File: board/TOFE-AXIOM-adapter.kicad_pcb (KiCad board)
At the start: 4 copper layers, 68.9 x 28.3 mm, 11 parts, among them CN1 C, U1 24AA01/24LC01B

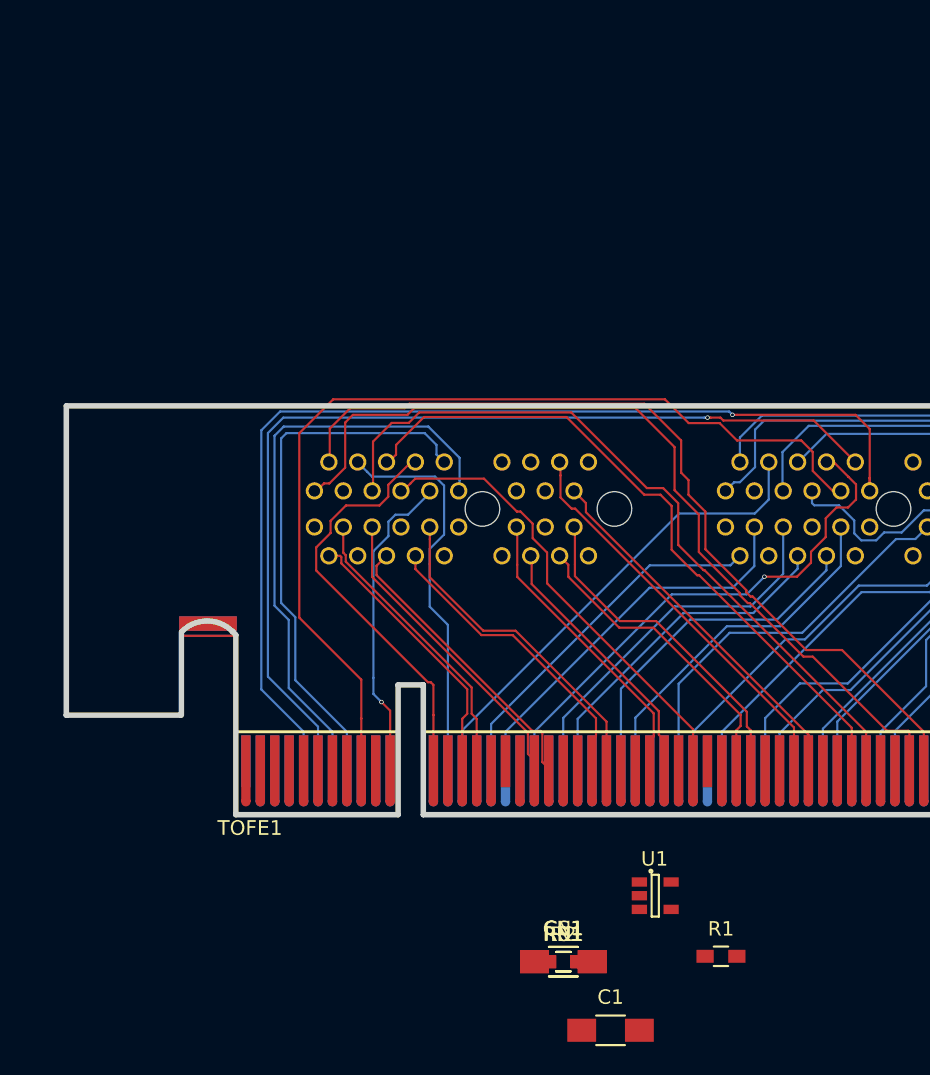
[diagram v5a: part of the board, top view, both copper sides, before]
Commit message: Adding more parts to the PCB.
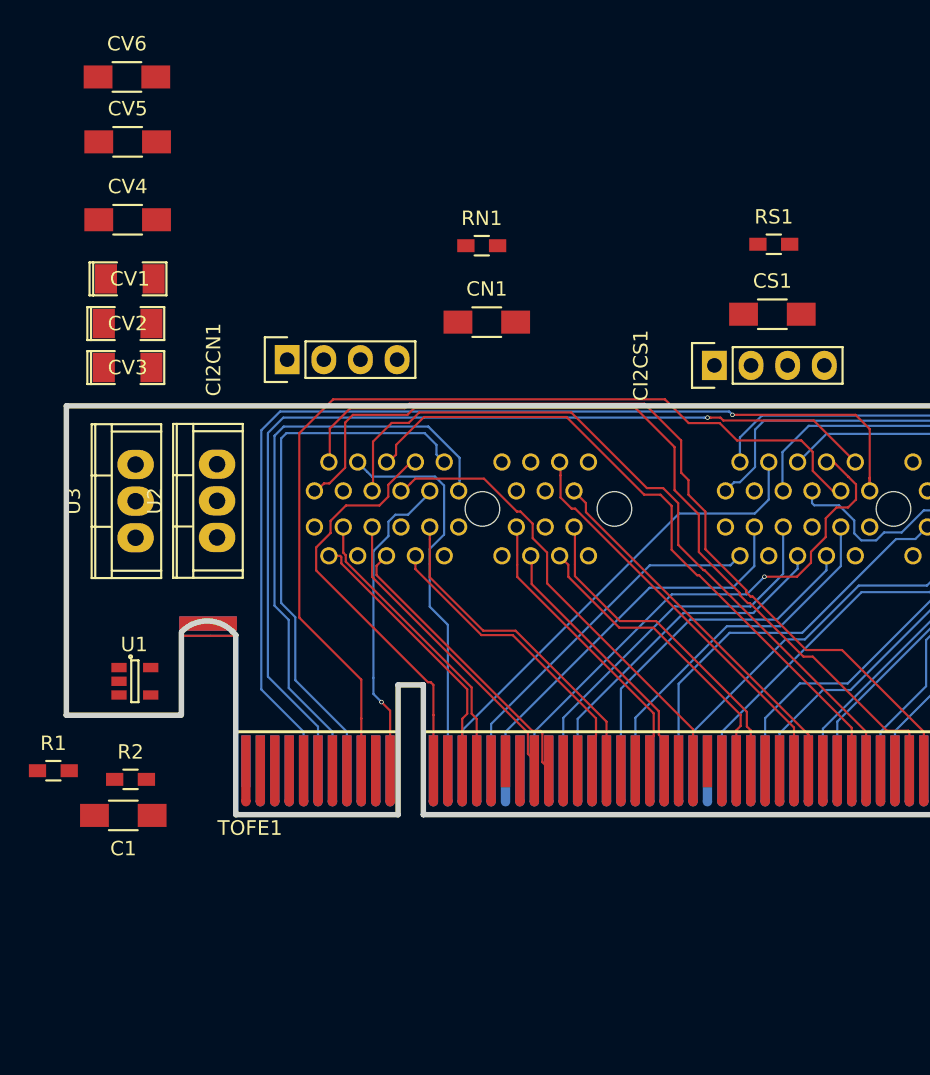
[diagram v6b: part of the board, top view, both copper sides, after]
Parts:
- added CI2CN1: CONN_01X04, Pin_Headers:Pin_Header_Straight_1x04, F.Cu at (177.6, 156.6)
- added CI2CS1: CONN_01X04, Pin_Headers:Pin_Header_Straight_1x04, F.Cu at (207.2, 157.0)
- added CV1: CP1, SMD_Packages:SMD-1206_Pol, F.Cu at (166.7, 151.0)
- added CV2: CP1, SMD_Packages:SMD-1206_Pol, F.Cu at (166.5, 154.1)
- added CV3: CP1, SMD_Packages:SMD-1206_Pol, F.Cu at (166.5, 157.2)
- added CV4: C, Capacitors_SMD:C_1206_HandSoldering, F.Cu at (166.5, 146.9)
- added CV5: C, Capacitors_SMD:C_1206_HandSoldering, F.Cu at (166.5, 141.5)
- added CV6: C, Capacitors_SMD:C_1206_HandSoldering, F.Cu at (166.4, 137.0)
- added U2: LM317T, Power_Integrations:TO-220, F.Cu at (172.7, 166.4)
- added U3: LM7805CT, Power_Integrations:TO-220, F.Cu at (167.1, 166.4)
- moved RS1 51.8 mm to (211.3, 148.6)
- moved RN1 50.0 mm to (191.1, 148.7)
- moved R1 48.0 mm to (161.3, 185.1)
- moved CS1 47.2 mm to (211.2, 153.4)
- moved CN1 44.7 mm to (191.4, 154.0)
- moved U1 39.0 mm to (167.0, 178.9)
- moved C1 36.9 mm to (166.2, 188.2), turned to 180 degrees
- moved R2 32.6 mm to (166.7, 185.7)

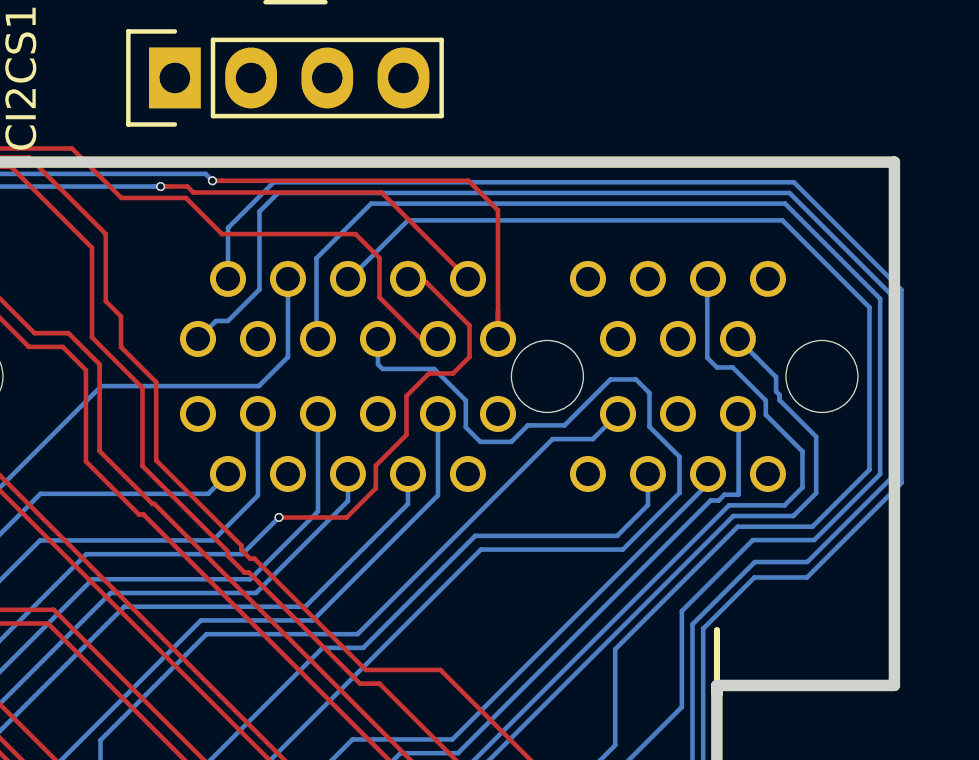
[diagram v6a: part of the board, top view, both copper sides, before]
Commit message: Fixed connector spacing to be 28.575 (rather then 28.500) spacing.
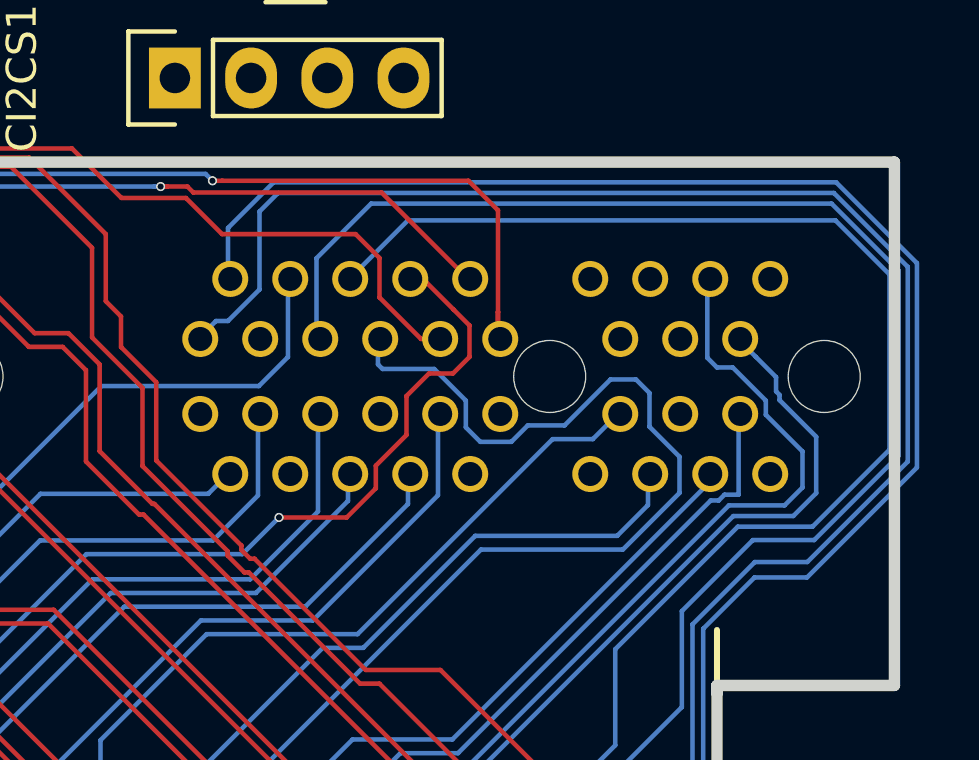
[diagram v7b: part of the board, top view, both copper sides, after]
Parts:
- moved SOUTH1 0.07 mm to (217.5, 166.9)
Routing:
- net /S_IO2: track 46.1 -> 47.7 mm
- net /S_IO1: track 50.0 -> 51.4 mm
- net /S_SDA: track 53.3 -> 54.6 mm
- net /S_SCL: track 51.4 -> 52.6 mm

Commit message: Starting to get length matching checking working.
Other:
- net class IO_NORTH_LM0.1 added: clearance 0.1524, trace_width 0.1524, via_dia 0.3048, via_drill 0.2032
- net class IO_SOUTH_LM0.1 added: clearance 0.1524, trace_width 0.1524, via_dia 0.3048, via_drill 0.2032
- net class LVDS_DP0.1/1.0 added: clearance 0.1524, trace_width 0.1524, via_dia 0.3048, via_drill 0.2032
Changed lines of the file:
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@@
     (links 152)
     (no_connects 103)
-    (area 159.172599 133.6226 231.628602 191.4274)
+    (area 159.172599 133.6226 232.143035 191.4274)
     (thickness 1.6)
     (drawings 25)
@@
     (uvia_dia 0.2032)
     (uvia_drill 0.1524)
-    (add_net /N_IO0)
-    (add_net /N_IO1)
-    (add_net /N_IO2)
-    (add_net /N_IO3)
-    (add_net /N_IO4)
-    (add_net /N_IO5)
-    (add_net /N_IO6)
-    (add_net /N_IO7)
-    (add_net /N_LVDS_0_N)
-    (add_net /N_LVDS_0_P)
-    (add_net /N_LVDS_1_N)
-    (add_net /N_LVDS_1_P)
-    (add_net /N_LVDS_2_N)
-    (add_net /N_LVDS_2_P)
-    (add_net /N_LVDS_3_N)
-    (add_net /N_LVDS_3_P)
-    (add_net /N_LVDS_4_N)
-    (add_net /N_LVDS_4_P)
-    (add_net /N_LVDS_5_N)
-    (add_net /N_LVDS_5_P)
-    (add_net /N_SCL)
-    (add_net /N_SDA)
     (add_net /PRSTN)
     (add_net /RESET)
@@
     (add_net /SMCLK)
     (add_net /SMDAT)
-    (add_net /S_IO0)
-    (add_net /S_IO1)
-    (add_net /S_IO2)
-    (add_net /S_IO3)
-    (add_net /S_IO4)
-    (add_net /S_IO5)
-    (add_net /S_IO6)
-    (add_net /S_IO7)
-    (add_net /S_LVDS_0_N)
-    (add_net /S_LVDS_0_P)
-    (add_net /S_LVDS_1_N)
-    (add_net /S_LVDS_1_P)
-    (add_net /S_LVDS_2_N)
-    (add_net /S_LVDS_2_P)
-    (add_net /S_LVDS_3_N)
-    (add_net /S_LVDS_3_P)
-    (add_net /S_LVDS_4_N)
-    (add_net /S_LVDS_4_P)
-    (add_net /S_LVDS_5_N)
-    (add_net /S_LVDS_5_P)
-    (add_net /S_SCL)
-    (add_net /S_SDA)
     (add_net /VCC12V)
     (add_net /VCC3V3)
@@
     (add_net "Net-(TOFE1-PadA33)")
   )
+  (net_class IO_NORTH_LM0.1 ""
+    (clearance 0.1524)
+    (trace_width 0.1524)
+    (via_dia 0.3048)
+    (via_drill 0.2032)
+    (uvia_dia 0.2032)
+    (uvia_drill 0.1524)
+    (add_net /N_IO0)
+    (add_net /N_IO1)
+    (add_net /N_IO2)
+    (add_net /N_IO3)
+    (add_net /N_IO4)
+    (add_net /N_IO5)
+    (add_net /N_IO6)
+    (add_net /N_IO7)
+    (add_net /N_SCL)
+    (add_net /N_SDA)
+  )
+  (net_class IO_SOUTH_LM0.1 ""
+    (clearance 0.1524)
+    (trace_width 0.1524)
+    (via_dia 0.3048)
+    (via_drill 0.2032)
+    (uvia_dia 0.2032)
+    (uvia_drill 0.1524)
+    (add_net /S_IO0)
+    (add_net /S_IO1)
+    (add_net /S_IO2)
+    (add_net /S_IO3)
+    (add_net /S_IO4)
+    (add_net /S_IO5)
+    (add_net /S_IO6)
+    (add_net /S_IO7)
+    (add_net /S_SCL)
+    (add_net /S_SDA)
+  )
+  (net_class LVDS_DP0.1/1.0 ""
+    (clearance 0.1524)
+    (trace_width 0.1524)
+    (via_dia 0.3048)
+    (via_drill 0.2032)
+    (uvia_dia 0.2032)
+    (uvia_drill 0.1524)
+    (add_net /N_LVDS_0_N)
+    (add_net /N_LVDS_0_P)
+    (add_net /N_LVDS_1_N)
+    (add_net /N_LVDS_1_P)
+    (add_net /N_LVDS_2_N)
+    (add_net /N_LVDS_2_P)
+    (add_net /N_LVDS_3_N)
+    (add_net /N_LVDS_3_P)
+    (add_net /N_LVDS_4_N)
+    (add_net /N_LVDS_4_P)
+    (add_net /N_LVDS_5_N)
+    (add_net /N_LVDS_5_P)
+    (add_net /S_LVDS_0_N)
+    (add_net /S_LVDS_0_P)
+    (add_net /S_LVDS_1_N)
+    (add_net /S_LVDS_1_P)
+    (add_net /S_LVDS_2_N)
+    (add_net /S_LVDS_2_P)
+    (add_net /S_LVDS_3_N)
+    (add_net /S_LVDS_3_P)
+    (add_net /S_LVDS_4_N)
+    (add_net /S_LVDS_4_P)
+    (add_net /S_LVDS_5_N)
+    (add_net /S_LVDS_5_P)
+  )
   (module Capacitors_SMD:C_1206_HandSoldering (layer F.Cu)
